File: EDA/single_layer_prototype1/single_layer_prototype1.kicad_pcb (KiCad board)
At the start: 2 copper layers, 108 x 85.7 mm, 2 parts, among them U1 CD74HC4067SM

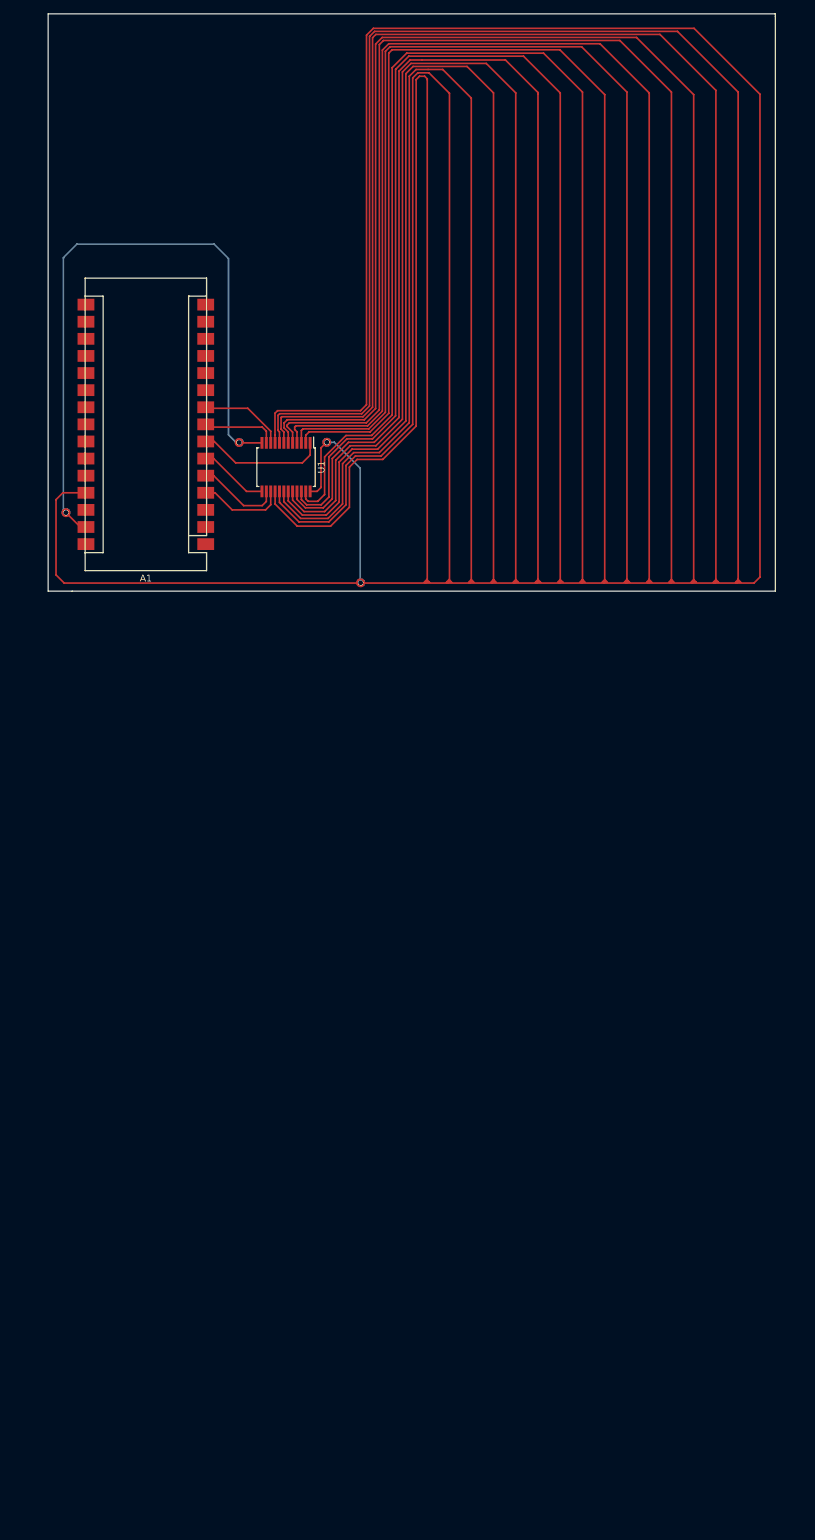
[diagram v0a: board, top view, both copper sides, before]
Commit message: update Arduino footprint
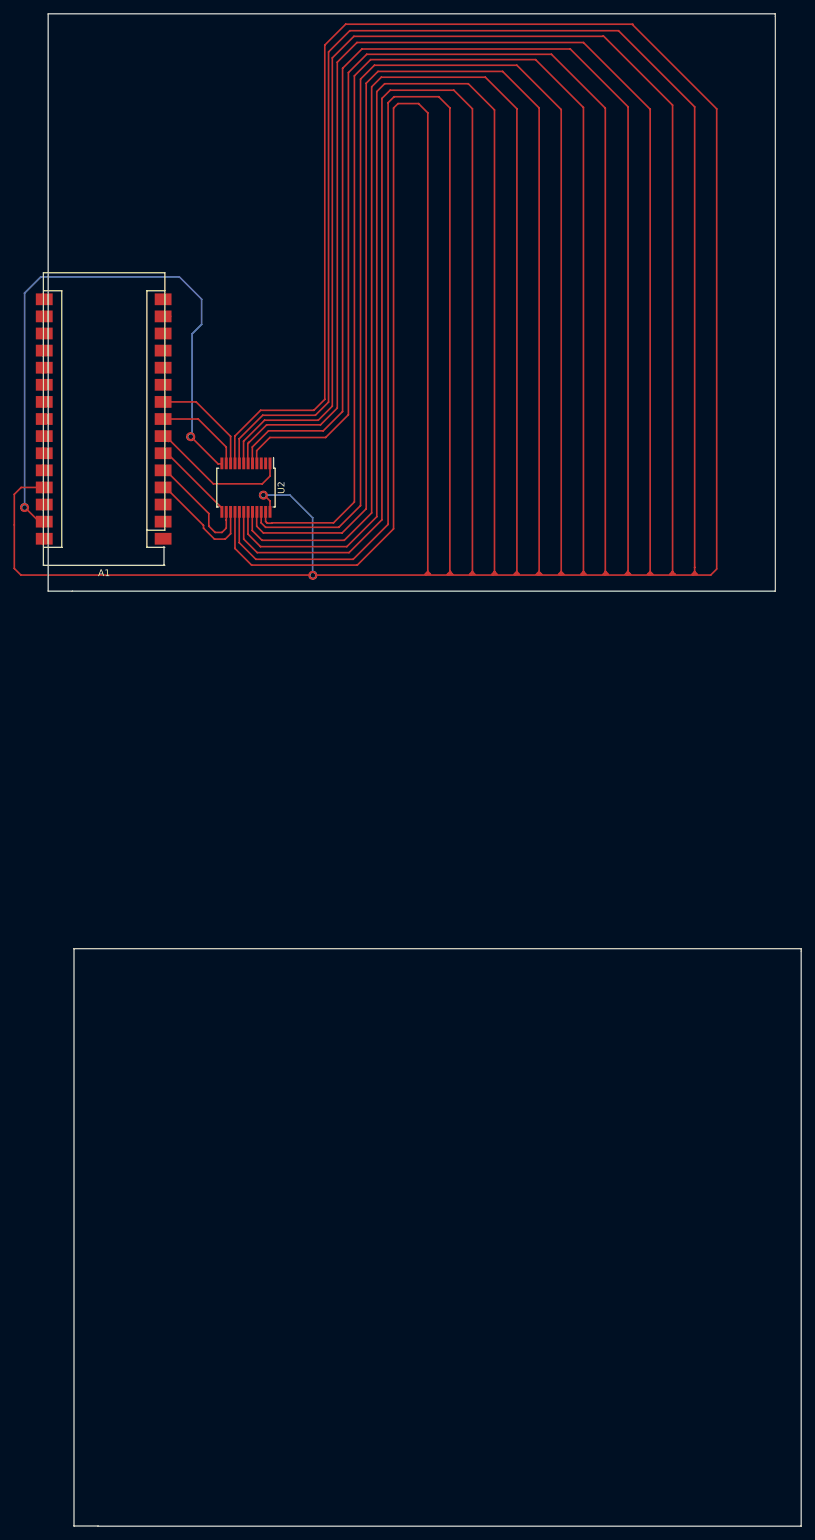
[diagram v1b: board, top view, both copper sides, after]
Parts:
- removed U1: CD74HC4067SM, Package_SO:SSOP-24_5.3x8.2mm_P0.65mm
- added U2: CD74HC4067SM, Package_SO:SSOP-24_5.3x8.2mm_P0.65mm, F.Cu at (112.7, 108.7)
- moved A1 6.25 mm to (99.3, 116.3)
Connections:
- A1 pad 10: unconnected-(A1-Pad10) -> (no net)
- A1 pad 11: unconnected-(A1-Pad11) -> (no net)
- A1 pad 12: unconnected-(A1-Pad12) -> (no net)
- A1 pad 13: unconnected-(A1-Pad13) -> (no net)
- A1 pad 14: unconnected-(A1-Pad14) -> (no net)
- A1 pad 5: Net-(A1-Pad5) -> (no net)
- A1 pad 6: Net-(A1-Pad6) -> (no net)
- A1 pad 8: Net-(A1-Pad8) -> (no net)
- A1 pad 9: Net-(A1-Pad9) -> (no net)
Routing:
- net Net-(A1-Pad27): track 3076.0 -> 2746.7 mm
- net (no net): track 0.00 -> 60.6 mm
- net Net-(A1-Pad5): track 12.7 -> 0.00 mm
- net Net-(A1-Pad9): track 11.0 -> 0.00 mm
- net Net-(A1-Pad6): track 10.5 -> 0.00 mm
- net Net-(A1-Pad8): track 9.20 -> 0.00 mm
- net GND: track 112.8 -> 108.2 mm
- net Net-(A1-Pad7): track 19.2 -> 22.2 mm
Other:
- board size 108 x 85.7 mm -> 111.8 x 224.6 mm
